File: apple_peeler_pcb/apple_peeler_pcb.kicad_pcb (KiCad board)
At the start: 2 copper layers, 131 parts, among them J1 BM03B-SRSS-TB, J2 BM03B-SRSS-TB, J3 HYC10-HDMIA19-600B, J4 HYC10-HDMIA19-600B, J5 USB_C_Receptacle_USB2.0_16P, Q1 2N7002, Q10 2N7002, Q11 2N7002, Q12 2N7002, Q13 2N7002, Q14 AO3401A, Q15 2N7002, Q16 AO3401A, Q17 2N7002, Q18 2N7002, Q2 2N7002, Q3 2N7002, Q4 2N7002, Q5 2N7002, Q6 2N7002, Q7 2N7002, Q8 2N7002, Q9 2N7002, SW1 SPST BTN, SW2 SPST BTN, SW3 SPST BTN, U1 W25Q16JVSS, U2 RP2040, U3 4066, U4 TPS562242, Y1 12MHz

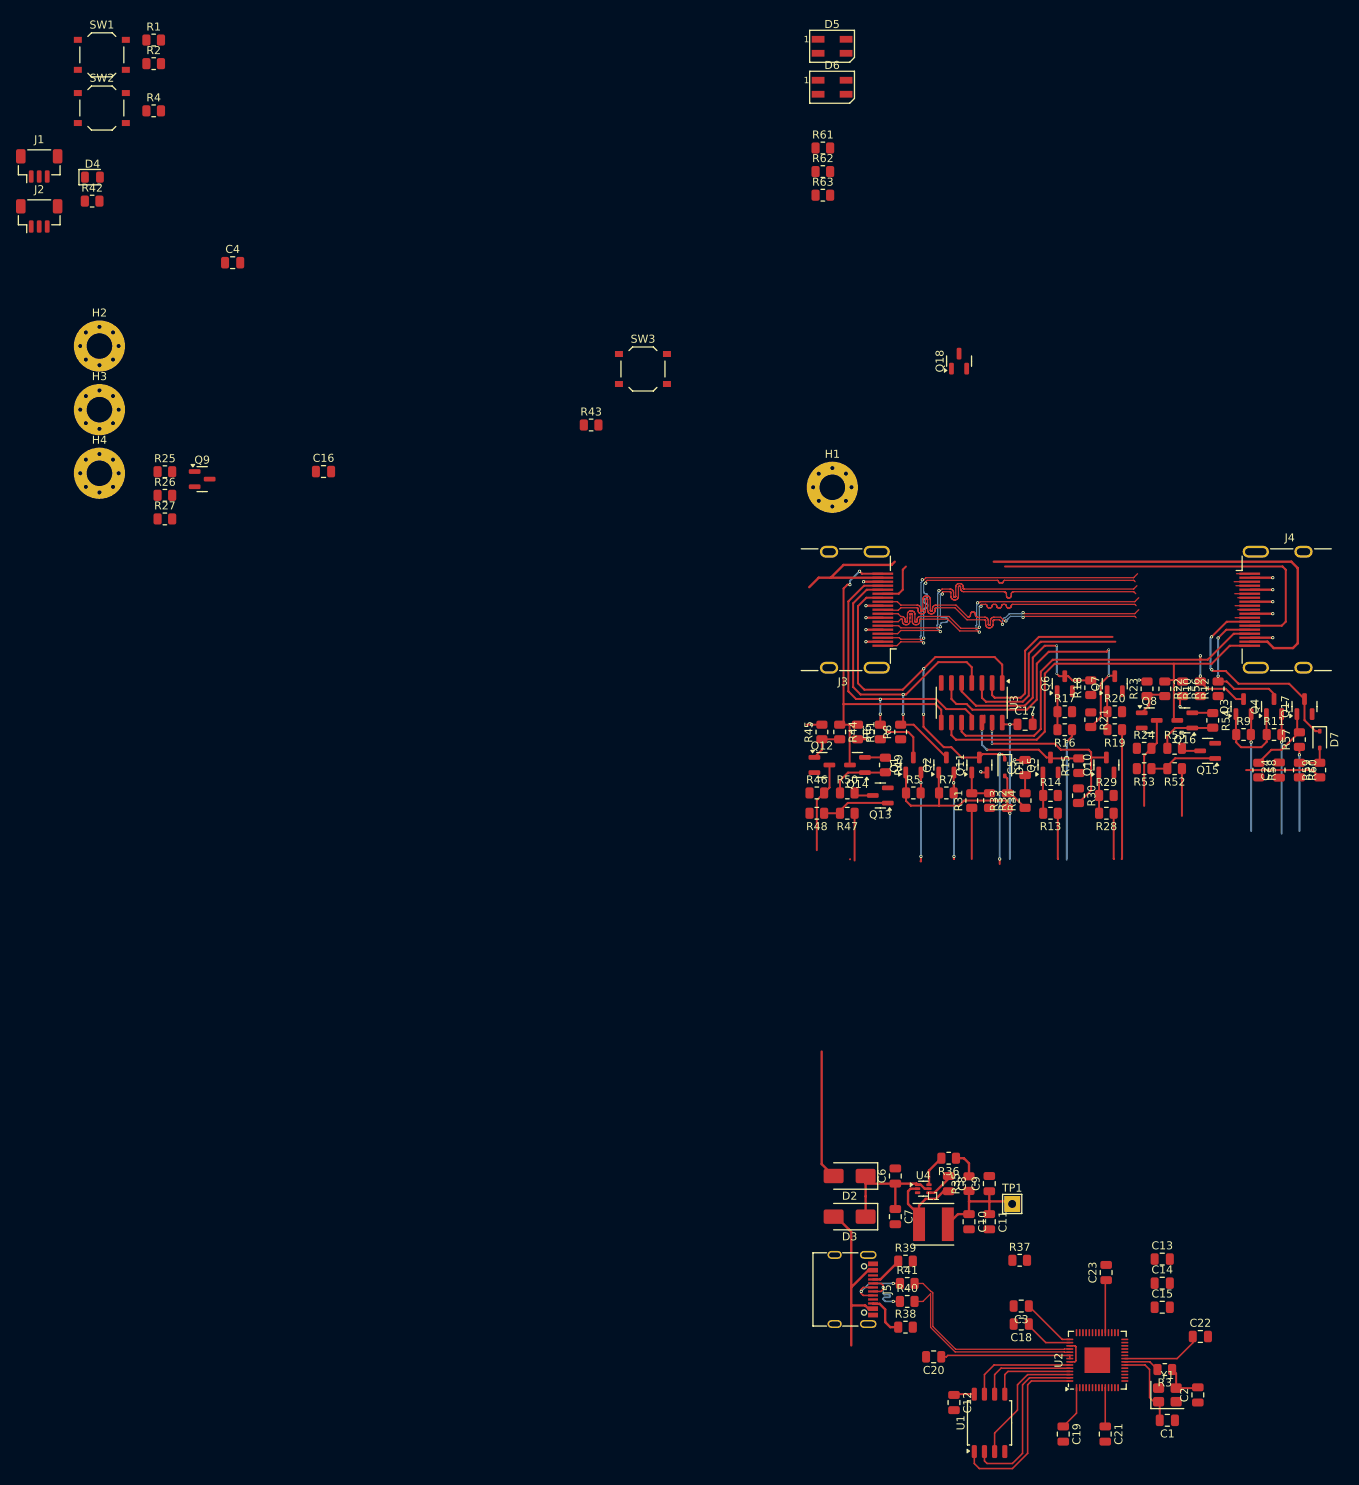
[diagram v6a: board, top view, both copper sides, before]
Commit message: vcc mon level shifter
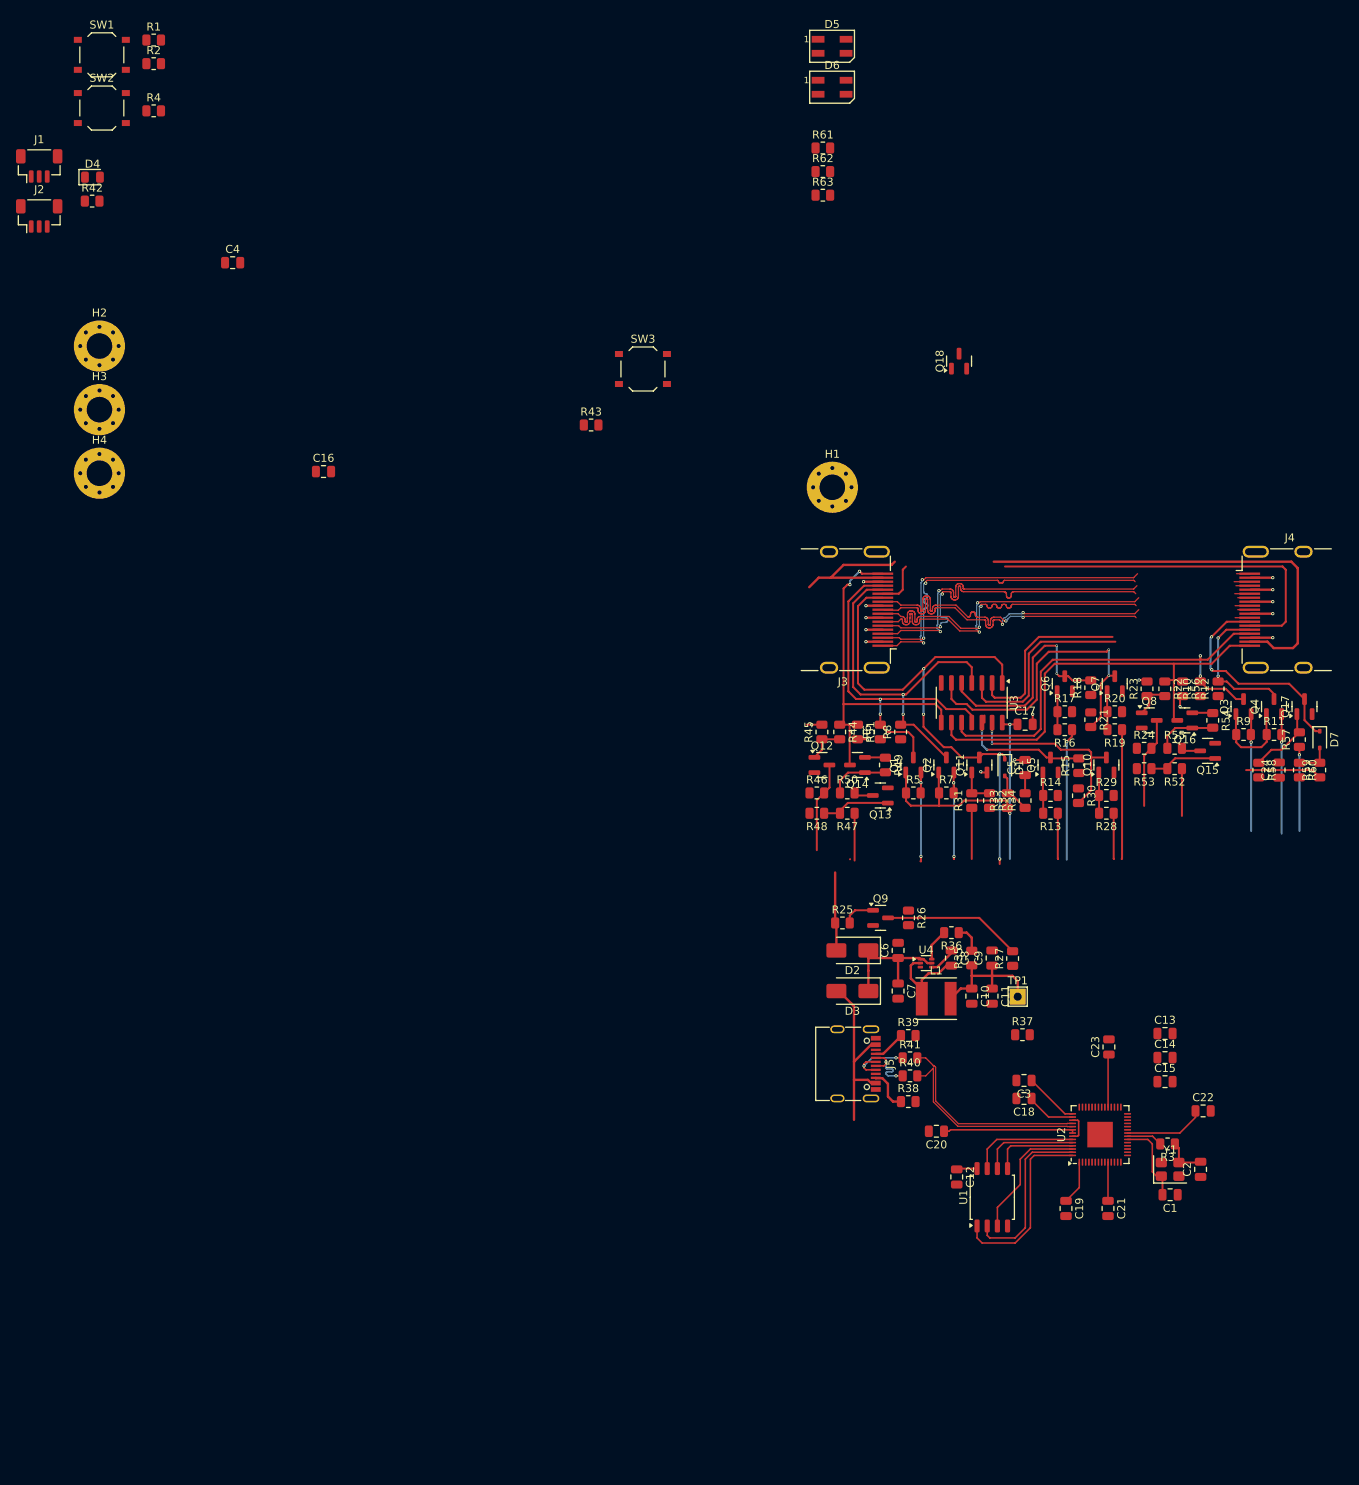
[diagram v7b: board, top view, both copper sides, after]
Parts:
- moved R27 119.4 mm to (179.7, 149.6), turned to 90 degrees
- moved R26 106.9 mm to (166.7, 144.5), turned to -90 degrees
- moved R25 101.8 mm to (158.5, 145.2)
- moved Q9 101.0 mm to (163.2, 144.5)
- moved C13 28.2 mm to (198.8, 159.0)
- moved C7 28.2 mm to (165.4, 153.7)
- moved C8 28.2 mm to (172.1, 149.5)
- moved C9 28.2 mm to (177.2, 149.5)
- moved D3 28.2 mm to (159.7, 153.7)
- moved R35 28.2 mm to (174.6, 149.5)
- moved U1 28.2 mm to (177.2, 179.4)
- moved C1 28.2 mm to (199.4, 179.1)
- moved C10 28.2 mm to (174.6, 154.3)
- moved C11 28.2 mm to (177.2, 154.3)
- moved C12 28.2 mm to (172.7, 176.9)
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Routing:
- net /HDMI passthrough/VCC_MON: track 0.00 -> 17.3 mm
- net /HDMI passthrough/HDMI_VCC: track 89.0 -> 82.6 mm
- net Net-(Q9-G): track 0.00 -> 4.11 mm
- net +3.3V: track 129.3 -> 131.7 mm

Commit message: rg | xargs sed goes brrr
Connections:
- net /HDMI passthrough/CEC_SINK_MON renamed /HDMI passthrough/CEC_B_MON
- net /HDMI passthrough/CEC_SINK_PULLDOWN renamed /HDMI passthrough/CEC_B_PULLDOWN
- net /HDMI passthrough/CEC_SRC_MON renamed /HDMI passthrough/CEC_A_MON
- net /HDMI passthrough/CEC_SRC_PULLDOWN renamed /HDMI passthrough/CEC_A_PULLDOWN
- net /HDMI passthrough/HDMI connectors/ARC_SINK renamed /HDMI passthrough/HDMI connectors/ARC_B
- net /HDMI passthrough/HDMI connectors/HPD_SINK renamed /HDMI passthrough/HDMI connectors/HPD_B
- net /HDMI passthrough/HDMI connectors/HPD_SRC renamed /HDMI passthrough/HDMI connectors/HPD_A
- net /HDMI passthrough/HPD_SINK_ASSERT renamed /HDMI passthrough/HPD_B_ASSERT
- net /HDMI passthrough/HPD_SINK_MON renamed /HDMI passthrough/HPD_B_MON
- net /HDMI passthrough/HPD_SRC_ASSERT renamed /HDMI passthrough/HPD_A_ASSERT
- net /HDMI passthrough/HPD_SRC_MON renamed /HDMI passthrough/HPD_A_MON
- net /HDMI passthrough/SCL_SINK_3V3 renamed /HDMI passthrough/SCL_B_3V3
- net /HDMI passthrough/SCL_SRC_3V3 renamed /HDMI passthrough/SCL_A_3V3
- net /HDMI passthrough/SDA_SINK_3V3 renamed /HDMI passthrough/SDA_B_3V3
- net /HDMI passthrough/SDA_SRC_3V3 renamed /HDMI passthrough/SDA_A_3V3
